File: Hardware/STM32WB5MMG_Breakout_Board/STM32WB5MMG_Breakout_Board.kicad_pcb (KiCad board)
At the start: 2 copper layers, 30.5 x 55.4 mm, 13 parts, among them J2 Conn_01x11_Pin, J7 VDD, U1 STM32WB5MMG

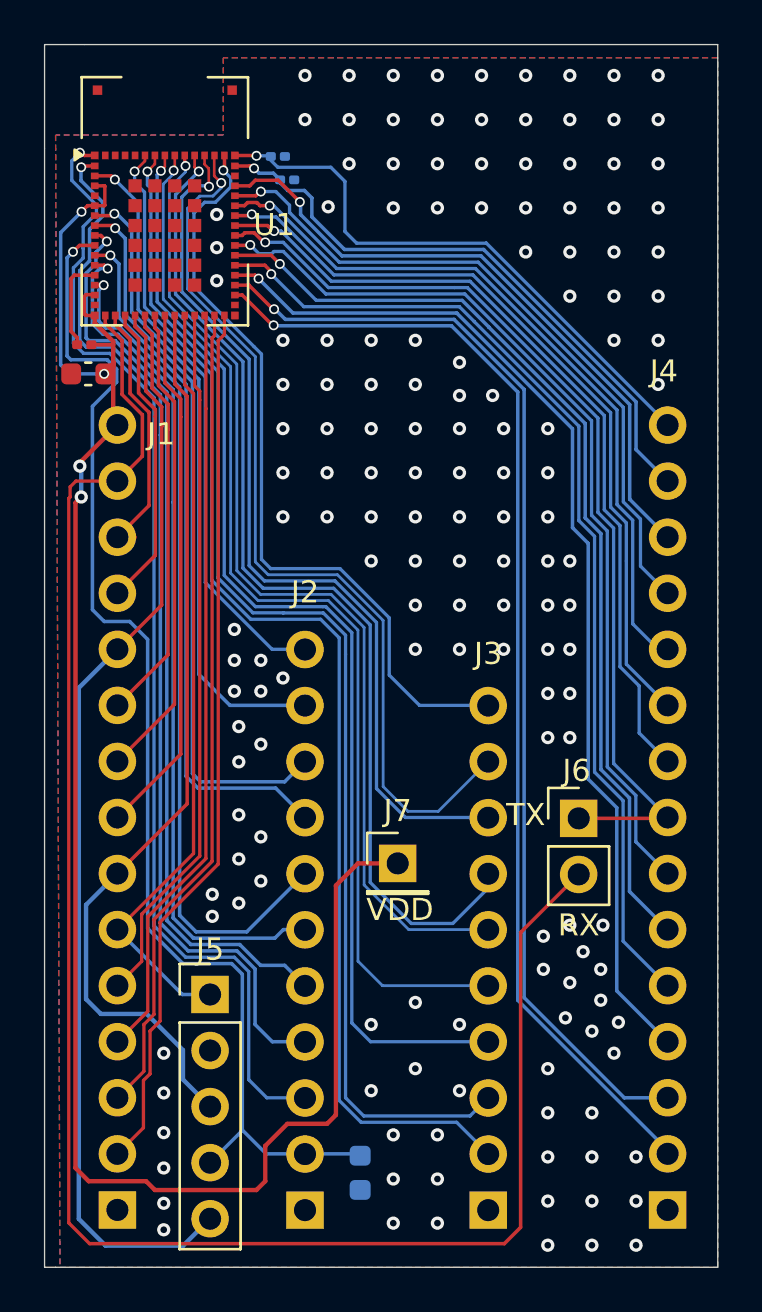
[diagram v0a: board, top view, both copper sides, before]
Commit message: updated stm32wb5mmg breakout board hardware
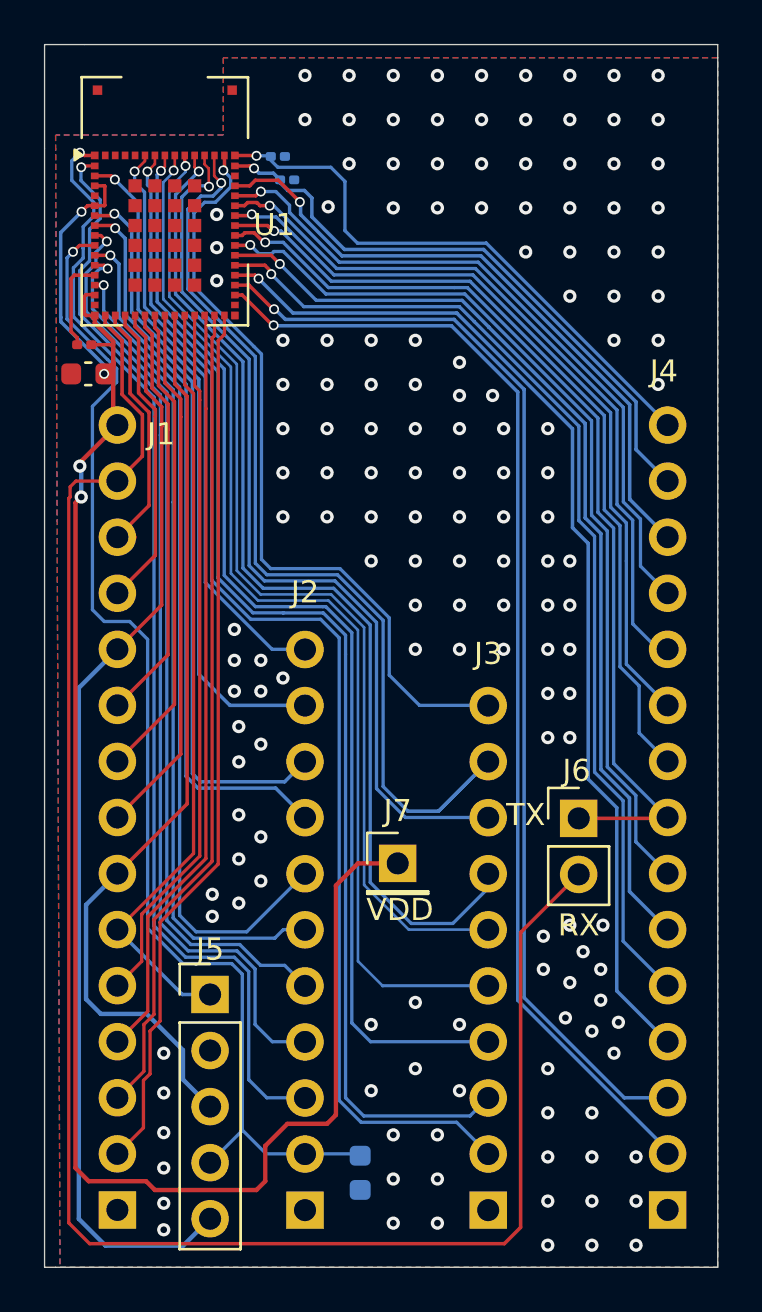
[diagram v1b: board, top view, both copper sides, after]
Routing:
- net PA6: track 48.6 -> 53.4 mm
- net PC4: track 41.5 -> 46.1 mm
- net NRST: track 56.1 -> 55.1 mm
- net VDD: track 83.8 -> 82.9 mm
- net PA1: track 48.2 -> 47.4 mm
- net PA2: track 51.9 -> 51.2 mm
- net PC1: track 41.5 -> 40.8 mm
- net PB8: track 38.0 -> 37.5 mm
